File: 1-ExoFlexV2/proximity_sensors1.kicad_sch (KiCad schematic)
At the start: 41 parts, among them U37 SN74LVC3G14DCUT_V2, U38 SN74LVC3G14DCUT_V2, U39 SN74LVC3G14DCUT_V2, U40 SN74LVC3G14DCUT_V2, U43 SN74LVC1G08DBVR, U44 SN74LVC1G08DBVR, U45 SN74LVC1G08DBVR, U46 SN74LVC1G08DBVR, U47 SN74LVC3G14DCUT_V2

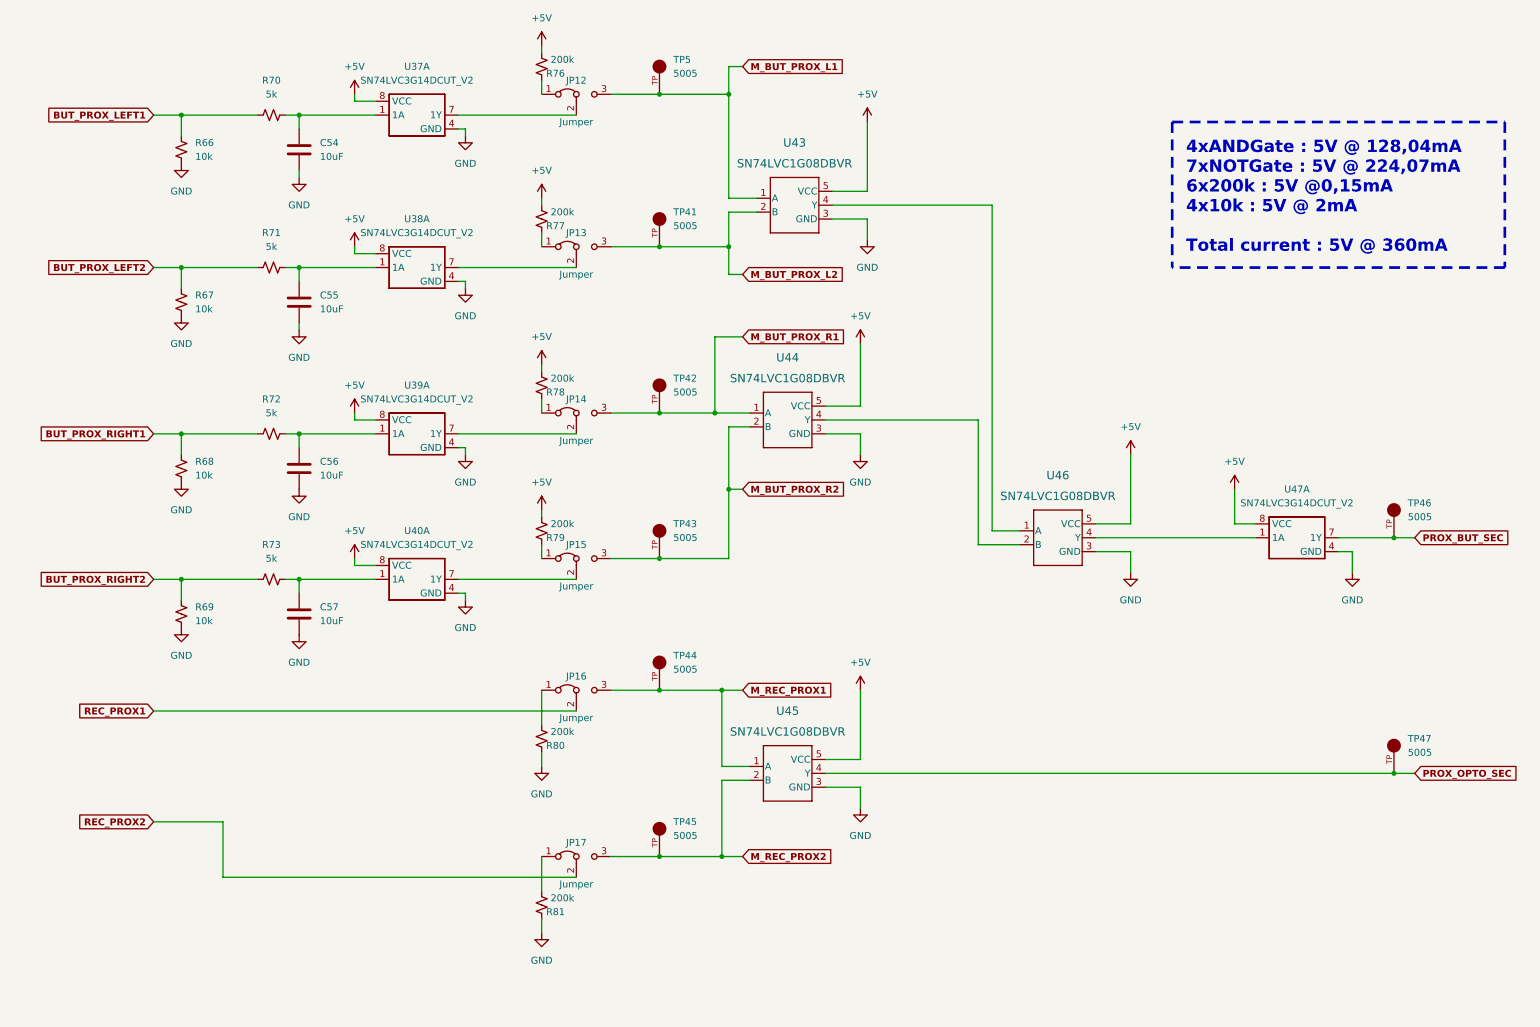
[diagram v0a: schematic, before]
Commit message: Chokes et RC
- Ajout des RF chokes
- Changement des résistance pour 0805
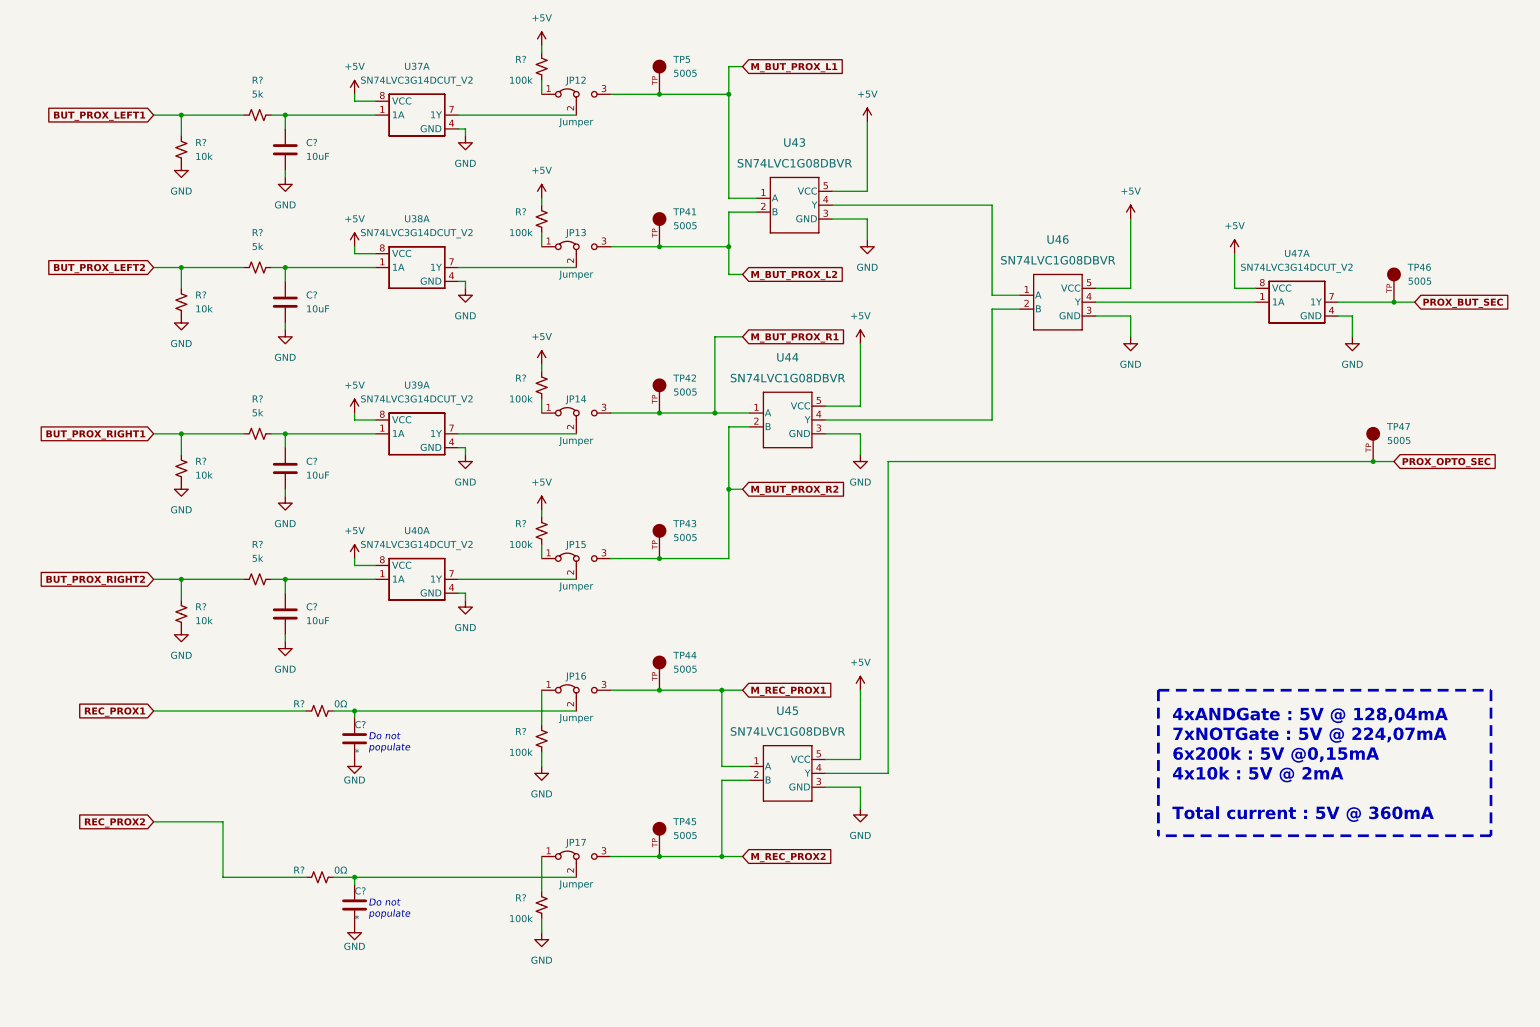
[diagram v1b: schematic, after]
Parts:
- removed C54, C55, C56, C57: 10uF, Capacitor_SMD:C_0603_1608Metric, symbol Device:C
- removed R66, R67, R68, R69: 10k, Resistor_SMD:R_0603_1608Metric, symbol Device:R_Small_US
- removed R70, R71, R72, R73: 5k, Resistor_SMD:R_0603_1608Metric, symbol Device:R_Small_US
- removed R76, R77, R78, R79, R80, R81: 200k, Resistor_SMD:R_0603_1608Metric, symbol Device:R_Small_US
- added C? (x4): 10uF, Capacitor_SMD:C_0805_2012Metric, symbol Device:C
- added C? (x2): *, Capacitor_SMD:C_0805_2012Metric, symbol Device:C
- added R? (x6): 100k, Resistor_SMD:R_0805_2012Metric, symbol Device:R_Small_US
- added R? (x4): 5k, Resistor_SMD:R_0805_2012Metric, symbol Device:R_Small_US
- added R? (x4): 10k, Resistor_SMD:R_0805_2012Metric, symbol Device:R_Small_US
- added R? (x2): 0Ω, Resistor_SMD:R_0805_2012Metric, symbol Device:R_Small_US
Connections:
- net +5V: now also R?.1, R?.1, R?.1, R?.1
- net BUT_PROX_LEFT1: now also R?.1, R?.1
- net BUT_PROX_LEFT2: now also R?.1, R?.1
- net BUT_PROX_RIGHT1: now also R?.1, R?.1
- net BUT_PROX_RIGHT2: now also R?.1, R?.1
- net GND: now also C?.2, C?.2, C?.2, C?.2, C?.2, C?.2, R?.2, R?.2, R?.2, R?.2, R?.2, R?.2
- net REC_PROX1: now also R?.1; no longer JP16.2 (C)
- net REC_PROX2: now also R?.1; no longer JP17.2 (C)
- net at U40.1 (1A): now also C?.1, R?.2
- net at U37.1 (1A): now also C?.1, R?.2
- net at JP16.1 (A): now also R?.1
- net at JP13.1 (A): now also R?.2
- net at JP17.1 (A): now also R?.1
- net at JP14.1 (A): now also R?.2
- net at U38.1 (1A): now also C?.1, R?.2
- net at U39.1 (1A): now also C?.1, R?.2
- net at JP15.1 (A): now also R?.2
- net at JP12.1 (A): now also R?.2
- new net: C?.1, JP17.2 (C), R?.2
- new net: C?.1, JP16.2 (C), R?.2
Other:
- note added: "Do not populate"
- moved on the sheet: TP46, TP47, U46, U47A

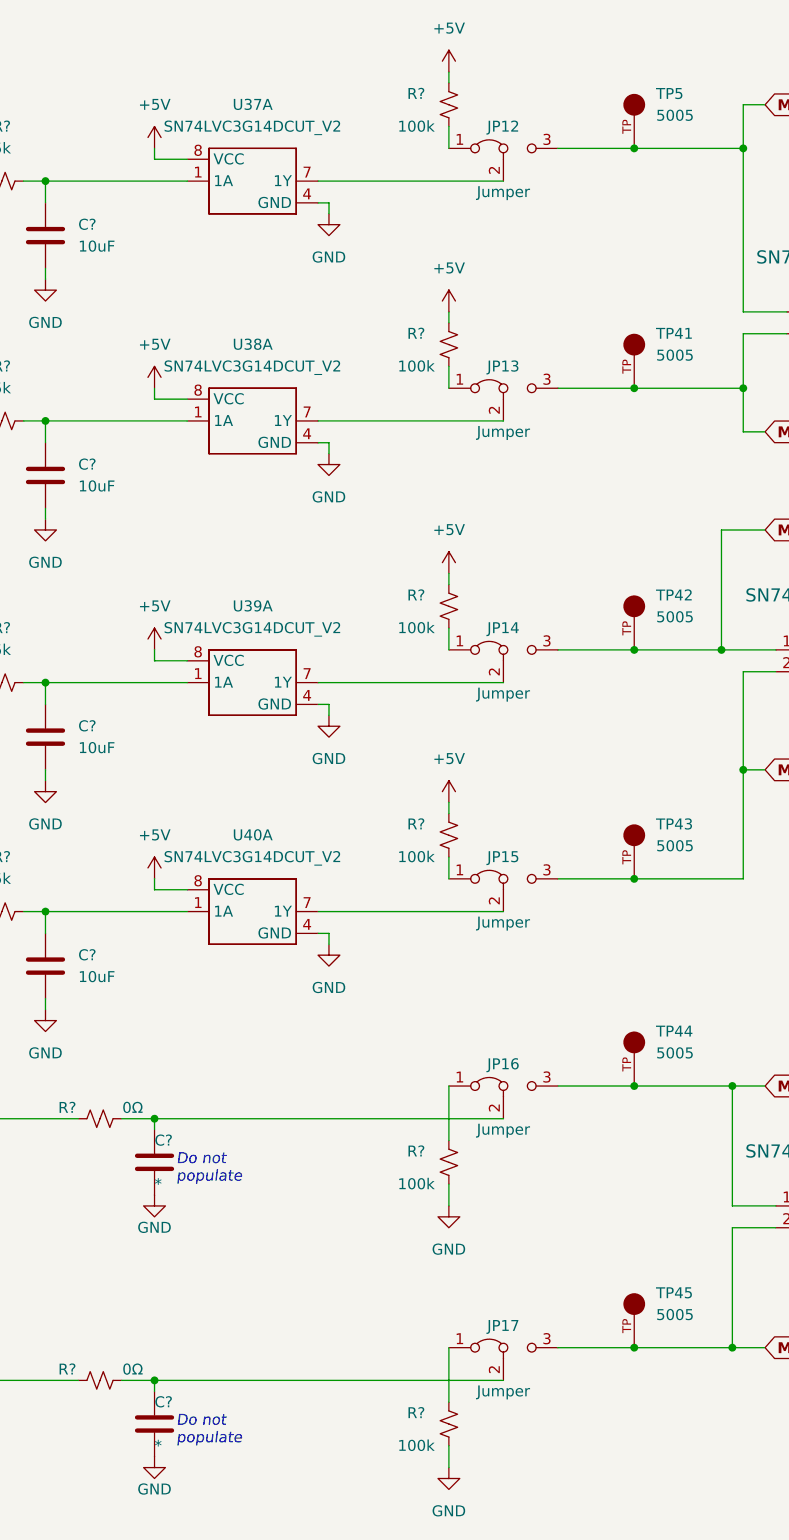
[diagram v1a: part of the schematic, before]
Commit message: Trimmer et jumper
-Changement de symbole de jumper
-Ajout des des trimmer aux endroits nécessaires
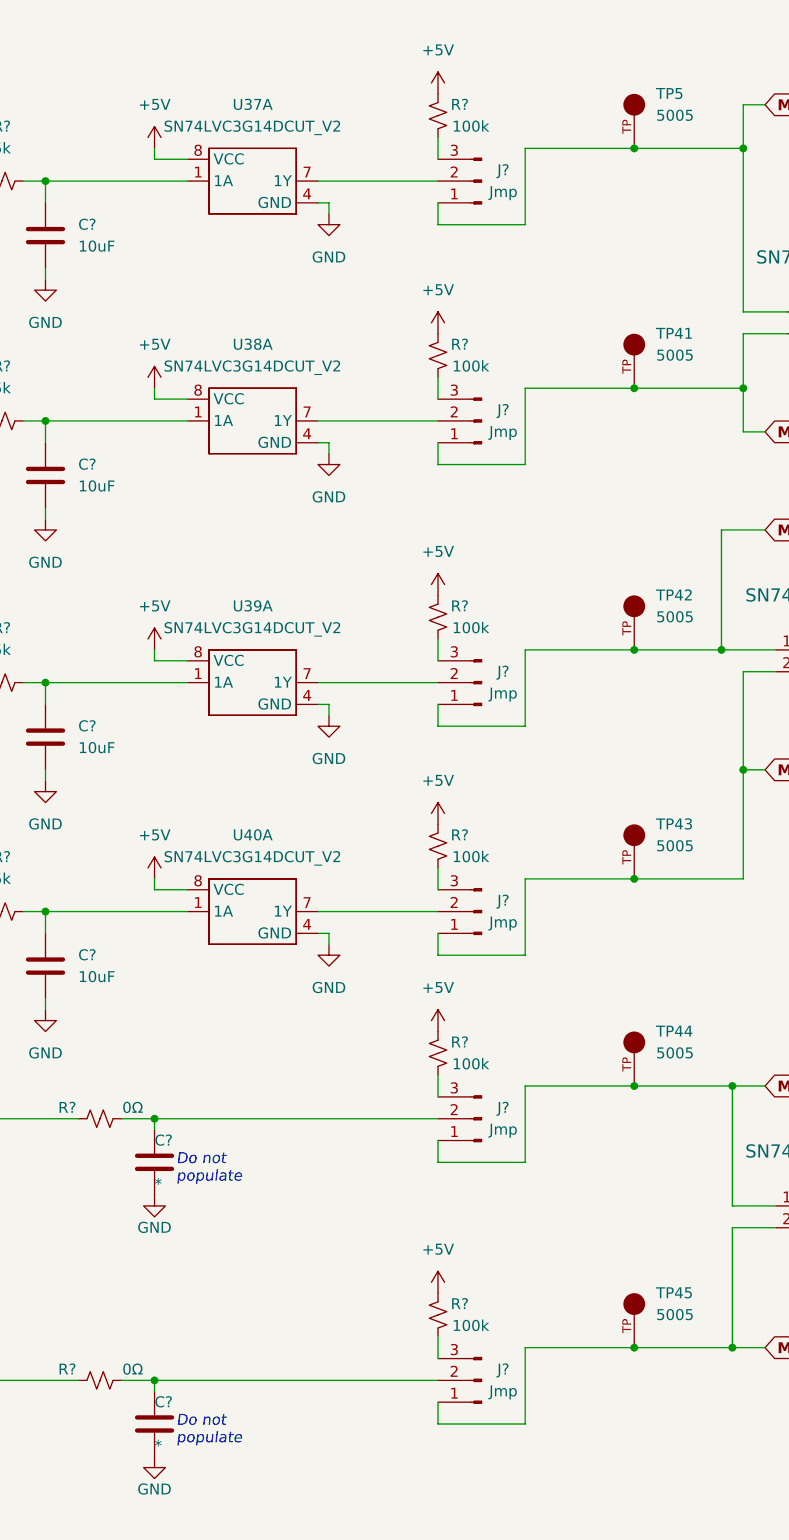
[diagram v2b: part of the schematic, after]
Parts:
- removed JP12, JP13, JP14, JP15, JP16, JP17: Jumper, Connector_PinHeader_2.54mm:PinHeader_1x03_P2.54mm_Vertical, symbol Jumper:Jumper_3_Bridged12
- removed R? (x6): 100k, Resistor_SMD:R_0805_2012Metric, symbol Device:R_Small_US
- added J? (x6): Jmp, symbol Connector:Conn_01x03_Male
- added R? (x6): 100k, Resistor_SMD:R_0805_2012Metric, symbol Device:R_Small_US
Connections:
- net +5V: now also R?.2, R?.2, R?.2, R?.2, R?.2, R?.2
- net M_BUT_PROX_L1: now also J?.1 (Pin_1)
- net M_BUT_PROX_L2: now also J?.1 (Pin_1)
- net M_BUT_PROX_R1: now also J?.1 (Pin_1)
- net M_BUT_PROX_R2: now also J?.1 (Pin_1)
- net M_REC_PROX1: now also J?.1 (Pin_1)
- net M_REC_PROX2: now also J?.1 (Pin_1)
- net at U40.7 (1Y): now also J?.2 (Pin_2)
- net at C?.1, R?.2: now also J?.2 (Pin_2) (x2)
- net at U37.7 (1Y): now also J?.2 (Pin_2)
- net at U39.7 (1Y): now also J?.2 (Pin_2)
- net at U38.7 (1Y): now also J?.2 (Pin_2)
- new net: J?.3 (Pin_3), R?.1 (x6)

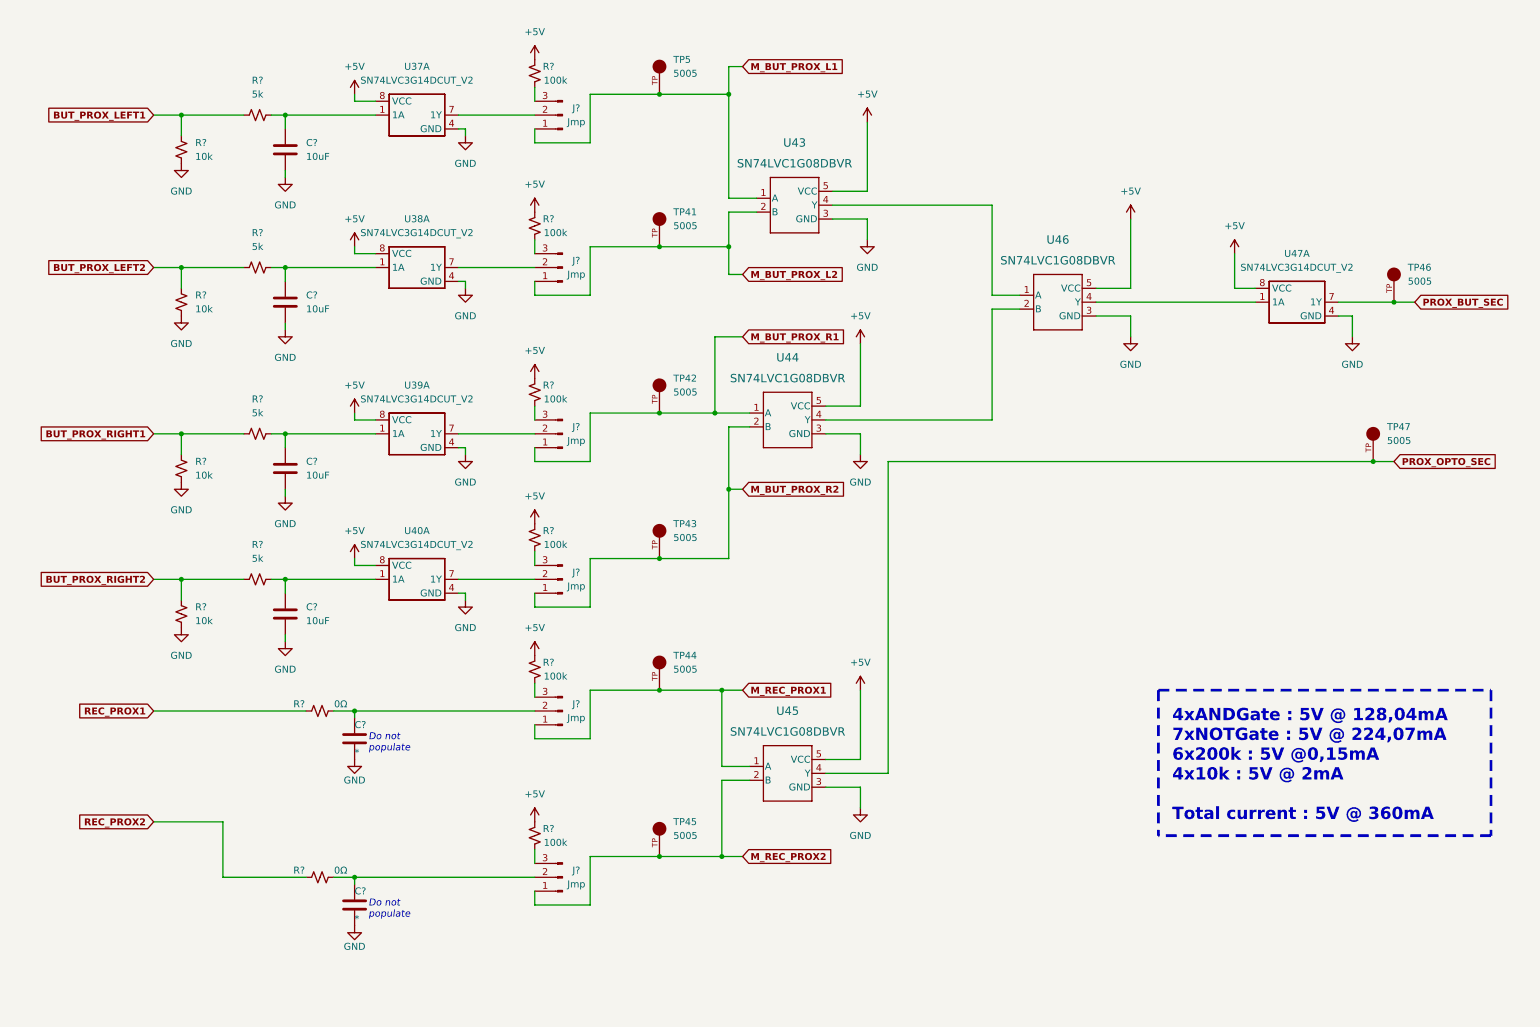
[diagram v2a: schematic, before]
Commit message: Test points et notes
- Ajout de tous les tests point nécessaires
-  Ajoute des sections de notes dans chaque page
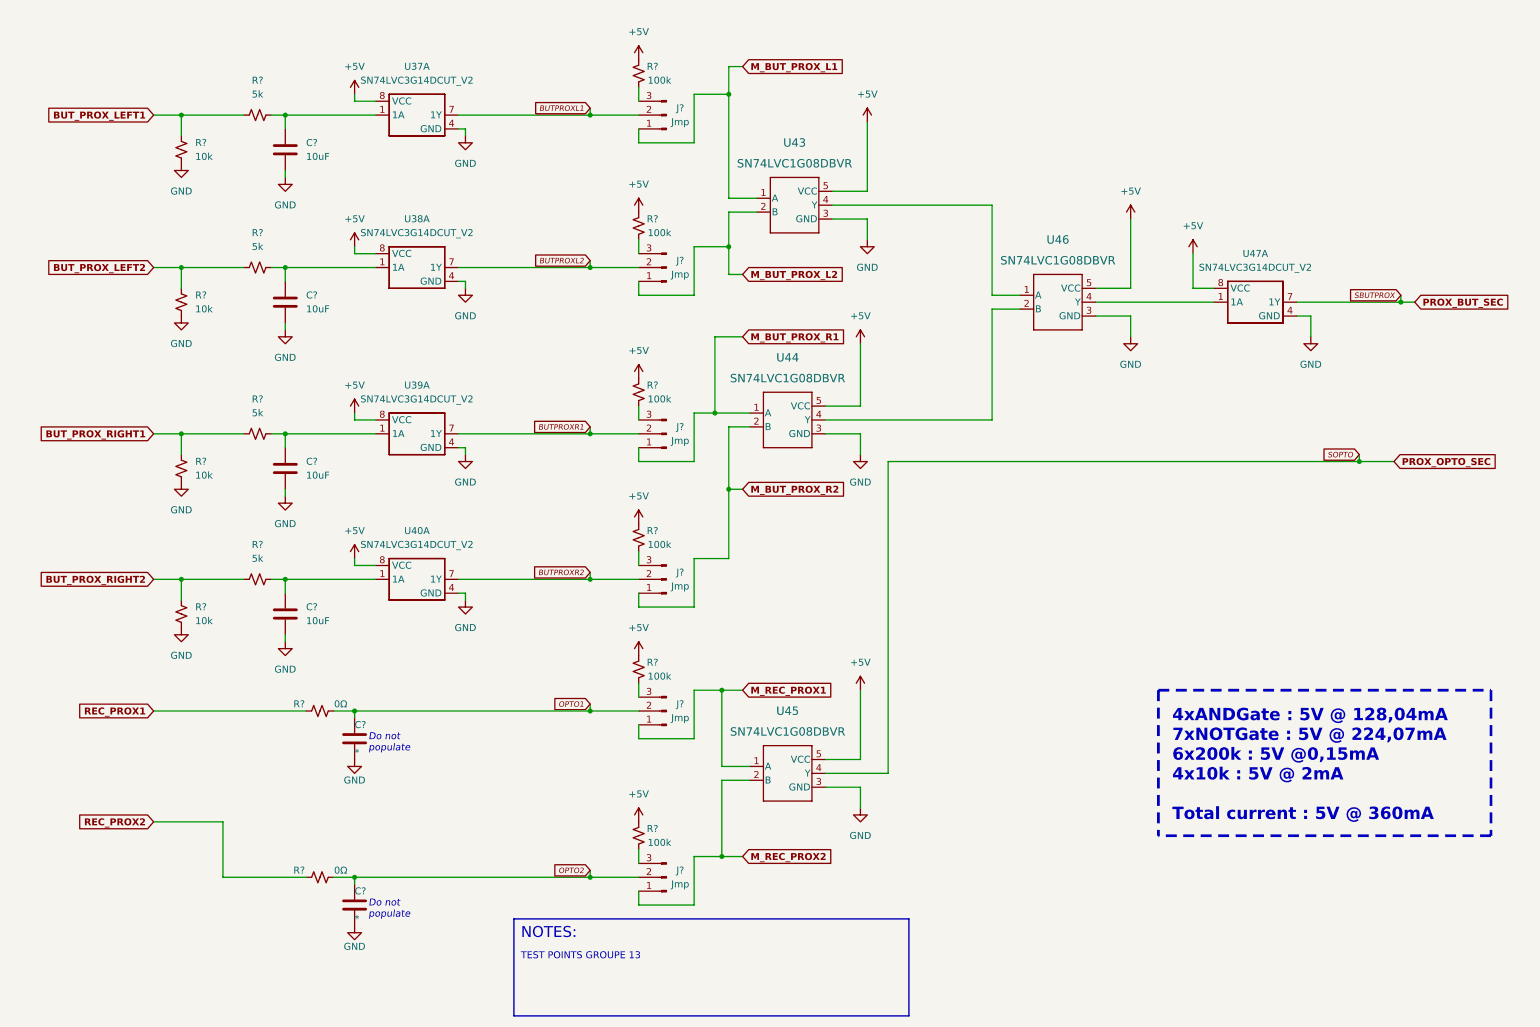
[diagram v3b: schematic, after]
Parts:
- removed TP41, TP42, TP43, TP44, TP45, TP46, TP47, TP5: 5005, FootPrint:KEYSTONE_5005, symbol SymLib:5005
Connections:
- net BUTPROXR2: now reaches J?.2 (Pin_2), U40.7 (1Y)
- net OPTO2: now reaches C?.1, J?.2 (Pin_2), R?.2
- net OPTO1: now reaches C?.1, J?.2 (Pin_2), R?.2
- net BUTPROXL1: now reaches J?.2 (Pin_2), U37.7 (1Y)
- net BUTPROXL2: now reaches J?.2 (Pin_2), U38.7 (1Y)
- net BUTPROXR1: now reaches J?.2 (Pin_2), U39.7 (1Y)
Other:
- note added: "NOTES:"
- note added: "TEST POINTS GROUPE 13"
- moved on the sheet: J?, R?, U47A
